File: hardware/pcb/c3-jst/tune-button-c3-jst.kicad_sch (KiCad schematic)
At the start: 38 parts, among them J1 USB-C, J2 LiPo, J3 Buttons, Q1 AO3401A, SW5 RESET, SW6 BOOT, U1 ESP32-C3-WROOM-02-N4, U2 SRV05-4, U3 TP4054, U4 RT9080-3.3, U5 SRV05-4

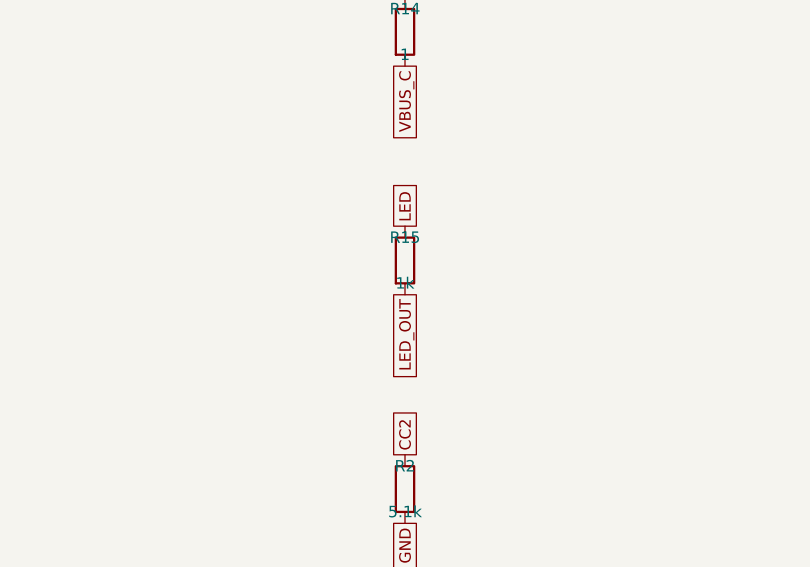
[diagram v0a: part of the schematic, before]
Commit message: pcb (c3-jst): round-1 audit fixes
JLC CPL rotates the 7-pin JST 180 degrees (JLC draws it pins-down; at 0 it would be
fitted backwards). A ground via 1.7 mm from U5's ground pin, where the ESD return ran
7.7 mm to the nearest via; the J3 pin legend moves to a column on the right so its
keepout leaves room. R15 330 ohm, so a lit button gets about 4 mA. Pin-1 mark clear
of J3's outline; TP1/TP2/U3 labels hidden. README covers the third board: JLC order
notes, rails, mounting, UART ground, the 3.6 V cutoff.
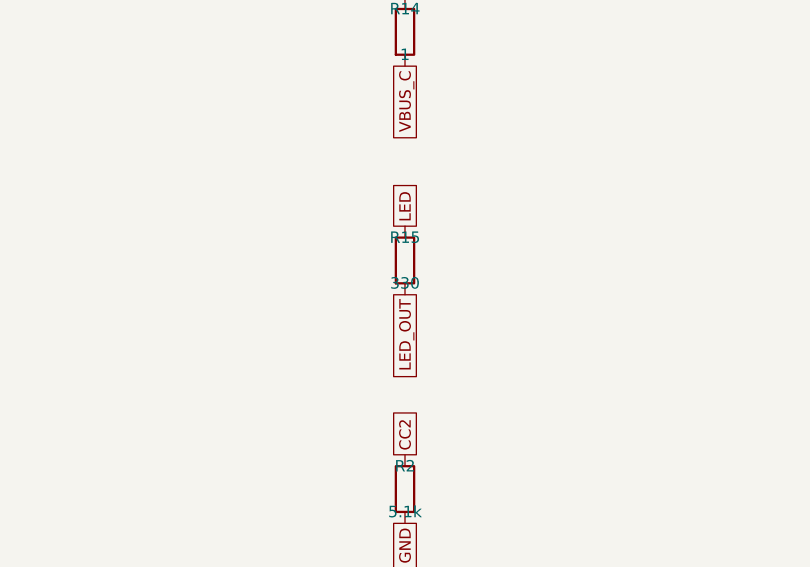
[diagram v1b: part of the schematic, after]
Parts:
- R15: value 1k -> 330; LCSC C21190 -> C23138
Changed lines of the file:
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@@
 			(effects (font (size 1.27 1.27)))
 		)
-		(property "Value" "1k"
+		(property "Value" "330"
 			(at 269.24 215.9 0)
 			(effects (font (size 1.27 1.27)))
@@
 			(effects (font (size 1.27 1.27)) (hide yes))
 		)
-		(property "LCSC" "C21190"
+		(property "LCSC" "C23138"
 			(at 269.24 223.52 0)
 			(effects (font (size 1.27 1.27)) (hide yes))

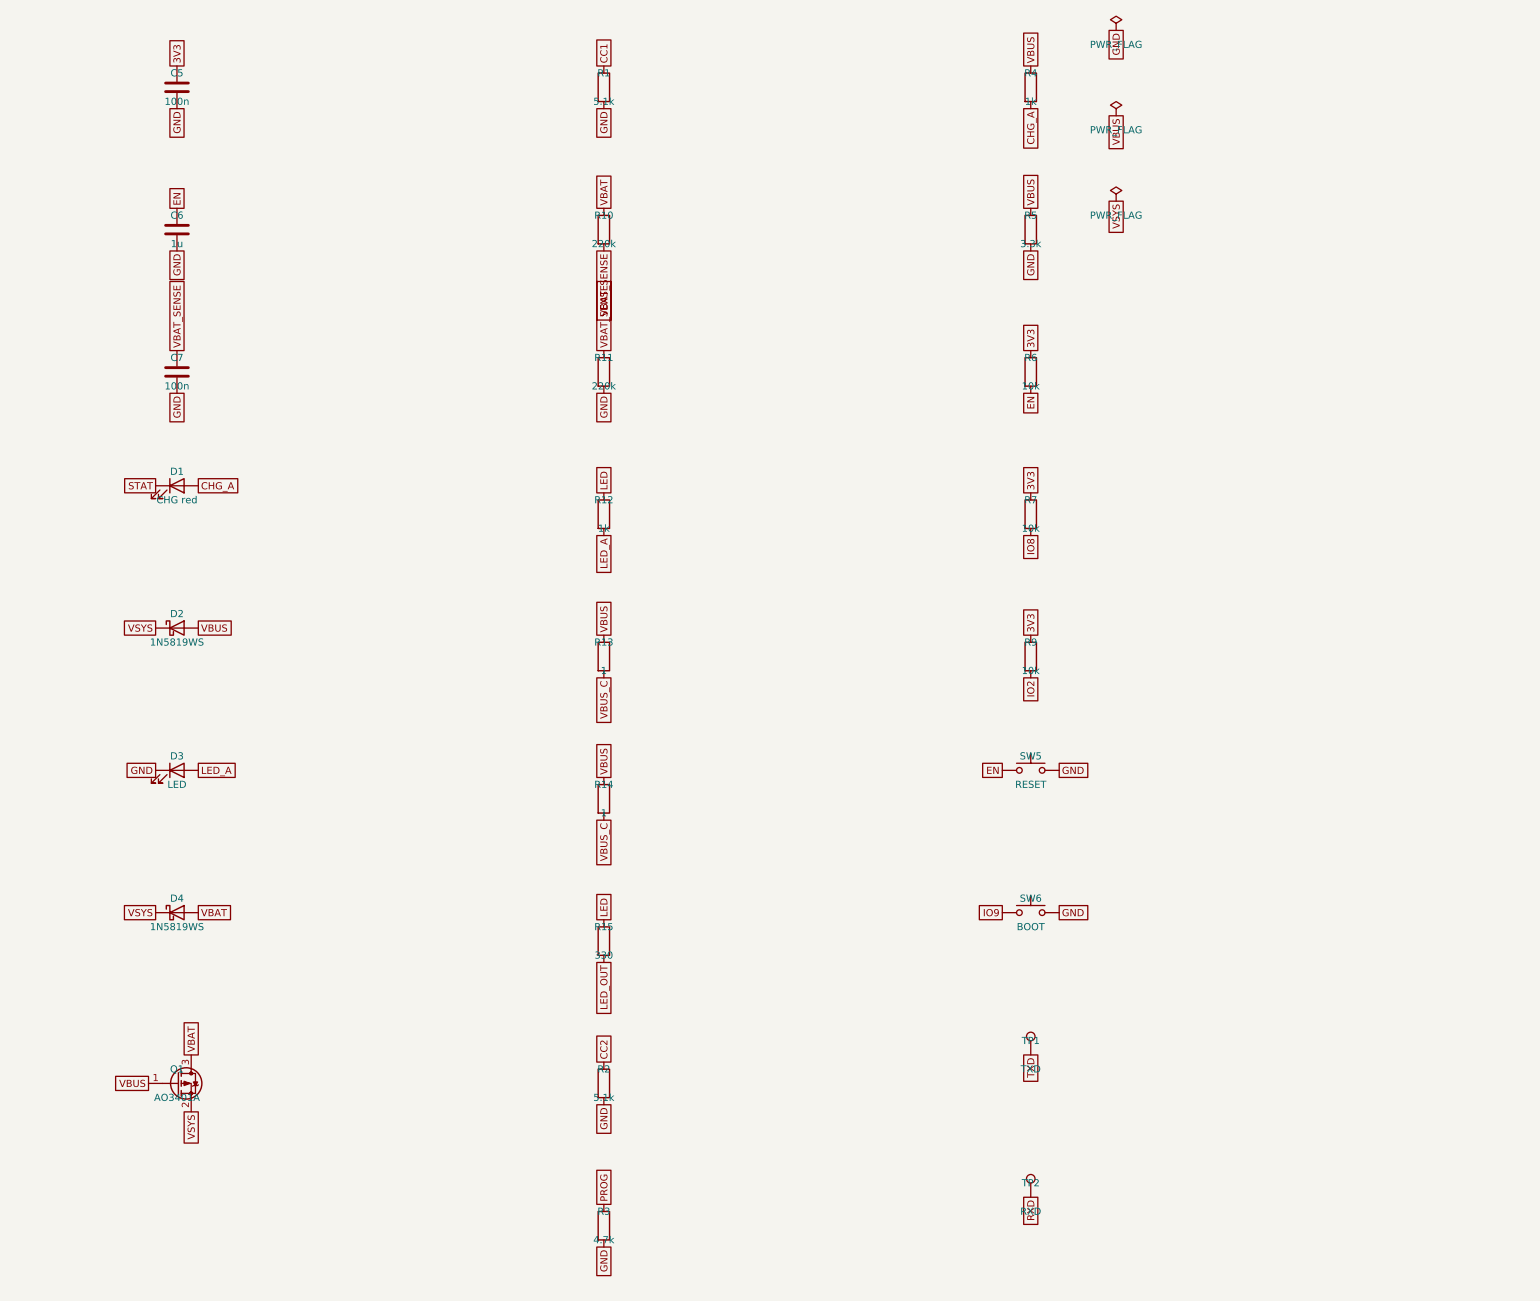
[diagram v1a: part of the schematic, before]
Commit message: pcb: c3-jst: RC damper (R16 1 ohm + C8 10 uF) at the RT9080 input, rerouted
sim12 had VSYS ringing to 6.6-6.7 V on a no-cell hot-plug against the RT9080's 6.5 V; sim13 puts
the damped worst case at 5.86 V. Panel rebuilt; README tab gaps and cutoff figures updated.
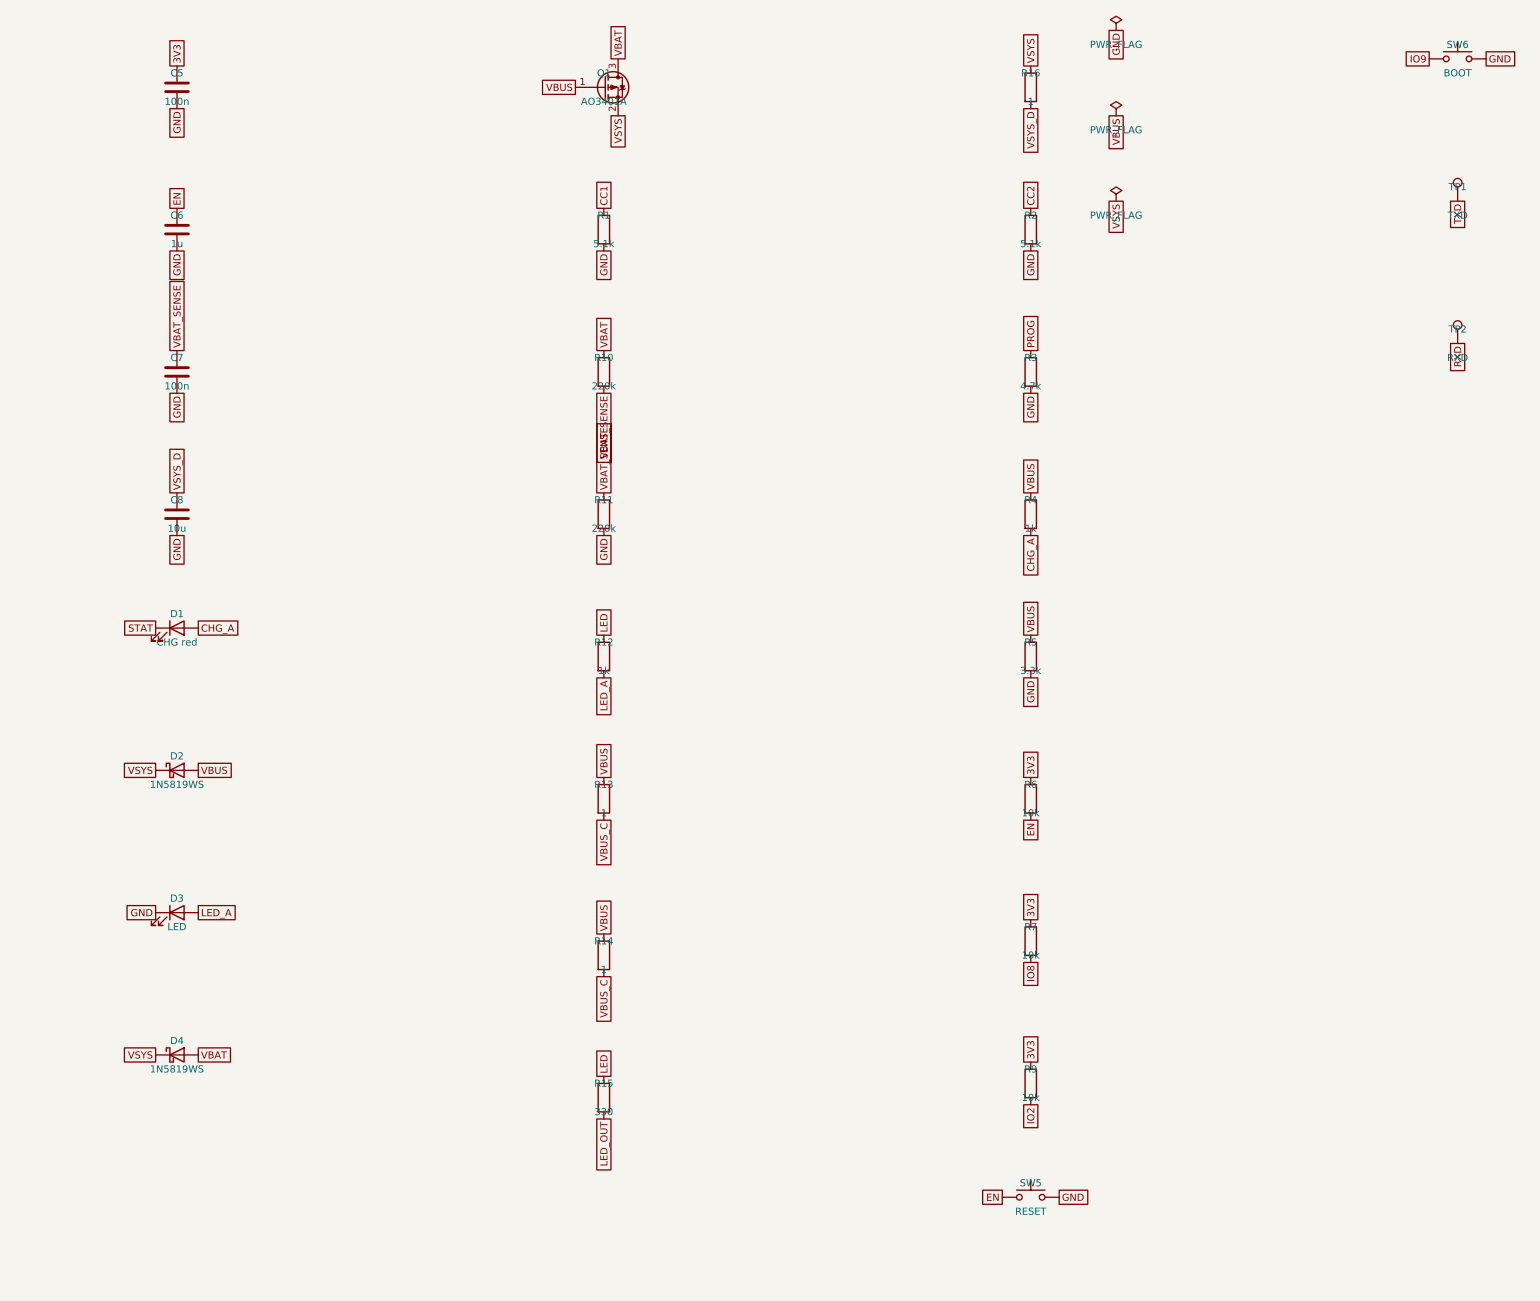
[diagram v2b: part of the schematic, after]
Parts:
- added C8: 10u, Capacitor_SMD:C_0805_2012Metric, symbol Device:C
- added R16: 1, Resistor_SMD:R_1206_3216Metric, symbol Device:R
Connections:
- net GND: now also C8.2
- net VSYS: now also R16.1
- new net VSYS_D: C8.1, R16.2
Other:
- moved on the sheet: D1, D2, D3, D4, Q1, R1, R10, R11, R12, R13, R14, R15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
